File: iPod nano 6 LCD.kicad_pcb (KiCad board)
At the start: 2 copper layers, 5 parts, among them U1 AP5724

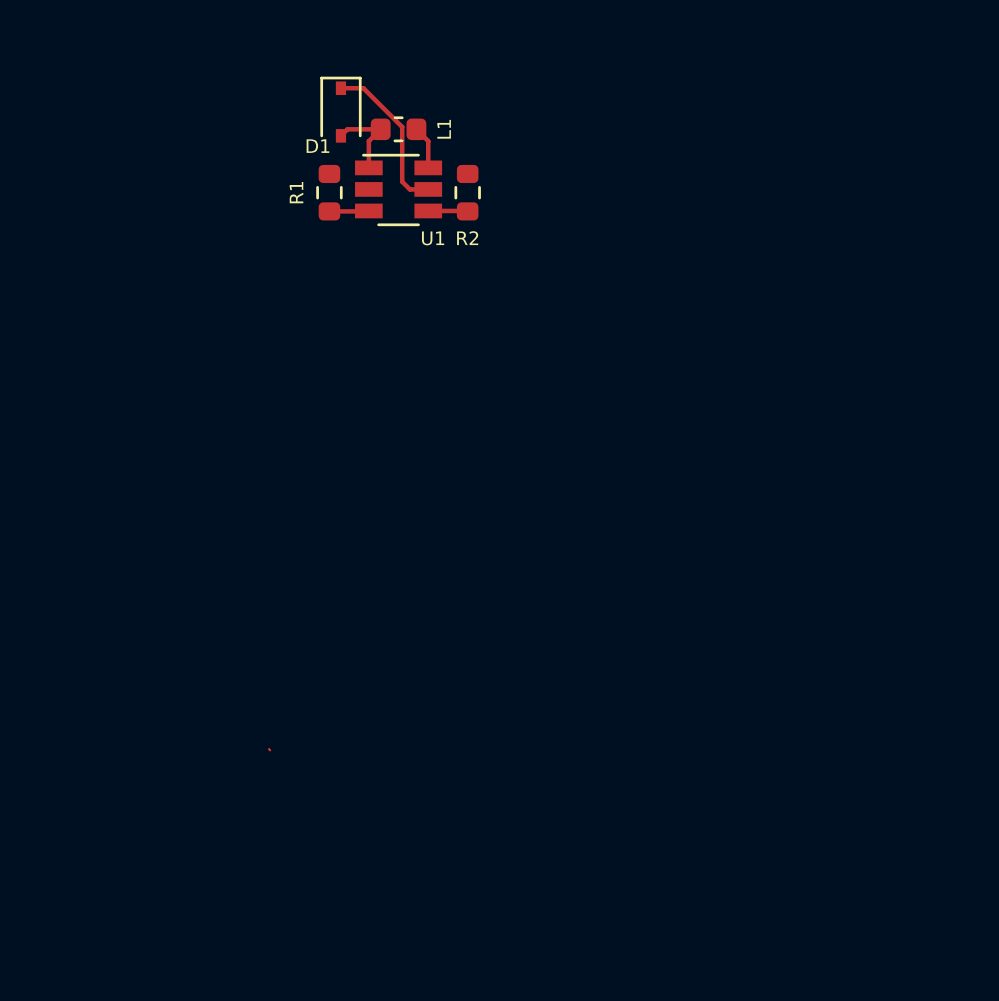
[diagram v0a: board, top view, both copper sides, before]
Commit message: Add USB and ATSAMD processor
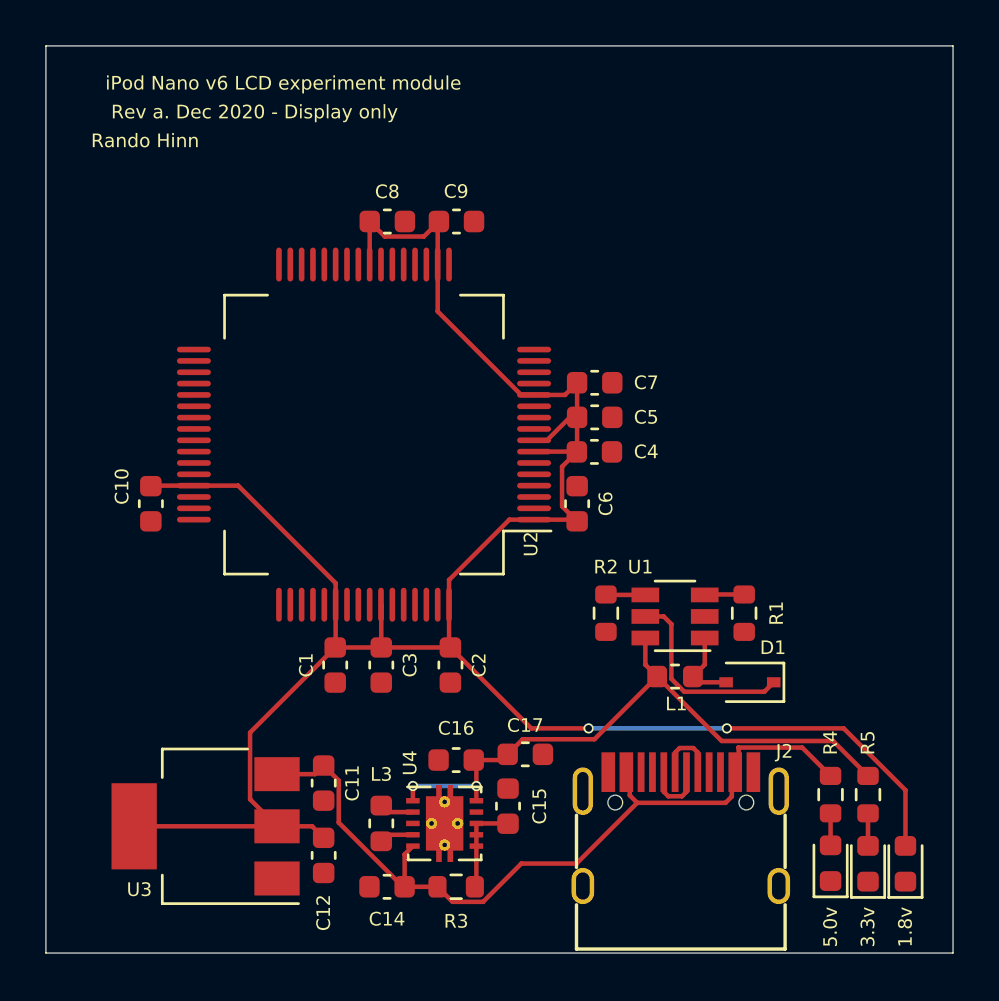
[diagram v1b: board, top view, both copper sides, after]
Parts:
- added C1: 1u, Capacitor_SMD:C_0603_1608Metric, F.Cu at (130.6, 85.1)
- added C10: 1u, Capacitor_SMD:C_0603_1608Metric, F.Cu at (122.4, 78.0)
- added C11: 1u, Capacitor_SMD:C_0603_1608Metric, F.Cu at (130.0, 90.3)
- added C12: 1u, Capacitor_SMD:C_0603_1608Metric, F.Cu at (130.0, 93.5)
- added C14: 1u, Capacitor_SMD:C_0603_1608Metric, F.Cu at (132.8, 94.9)
- added C15: .1u, Capacitor_SMD:C_0603_1608Metric, F.Cu at (138.2, 91.3)
- added C16: 10u, Capacitor_SMD:C_0603_1608Metric, F.Cu at (135.9, 89.3)
- added C17: 10u, Capacitor_SMD:C_0603_1608Metric, F.Cu at (138.9, 89.0)
- added C2: 1u, Capacitor_SMD:C_0603_1608Metric, F.Cu at (135.6, 85.1)
- added C3: 1u, Capacitor_SMD:C_0603_1608Metric, F.Cu at (132.6, 85.1)
- added C4: 1u, Capacitor_SMD:C_0603_1608Metric, F.Cu at (142.0, 75.7)
- added C5: 1u, Capacitor_SMD:C_0603_1608Metric, F.Cu at (142.0, 74.2)
- added C6: 1u, Capacitor_SMD:C_0603_1608Metric, F.Cu at (141.2, 78.0)
- added C7: 1u, Capacitor_SMD:C_0603_1608Metric, F.Cu at (142.0, 72.6)
- added C8: 1u, Capacitor_SMD:C_0603_1608Metric, F.Cu at (132.9, 65.5)
- added C9: 1u, Capacitor_SMD:C_0603_1608Metric, F.Cu at (135.9, 65.5)
- added D2: +5V, LED_SMD:LED_0603_1608Metric, F.Cu at (152.4, 93.8)
- added D3: +1.8V, LED_SMD:LED_0603_1608Metric, F.Cu at (155.7, 93.9)
- added D4: +3.3v, LED_SMD:LED_0603_1608Metric, F.Cu at (154.1, 93.9)
- added J2: USB_C_Receptacle_USB2.0, iPod nano 6 LCD:USB_C_Receptacle_GT-USB-7010, F.Cu at (145.8, 93.0)
- added L3: 2.2uH, Inductor_SMD:L_0603_1608Metric, F.Cu at (132.6, 92.1)
- added R3: 100, Resistor_SMD:R_0603_1608Metric, F.Cu at (135.9, 94.9)
- added R4: 16, Resistor_SMD:R_0603_1608Metric, F.Cu at (152.4, 90.8)
- added R5: 8, Resistor_SMD:R_0603_1608Metric, F.Cu at (154.1, 90.8)
- added U2: ATSAM3SD8BA-AU, iPod nano 6 LCD:QFP-64_12x12_Pitch0.5mm, F.Cu at (131.8, 74.9)
- added U3: AZ1117-1.8, Package_TO_SOT_SMD:SOT-223-3_TabPin2, F.Cu at (124.8, 92.2)
- added U4: TPS63001, Package_SON:Texas_DRC0010J_ThermalVias, F.Cu at (135.4, 92.1)
- moved D1 30.9 mm to (148.8, 85.9), turned to 180 degrees
- moved L1 27.0 mm to (145.5, 85.6), turned to 0 degrees
- moved R1 26.0 mm to (148.6, 82.8), turned to 270 degrees
- moved U1 22.4 mm to (145.5, 82.9), turned to 180 degrees
- moved R2 19.5 mm to (142.5, 82.8), turned to 270 degrees
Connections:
- net +3V0 renamed +3V3
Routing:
- net VDDIN: track 0.00 -> 101.9 mm, vias 0 -> 2
- net +5V: track 0.00 -> 35.9 mm
- net +3V3: track 1.92 -> 27.9 mm, vias 0 -> 2
- net Net-(C15-Pad1): track 0.00 -> 4.22 mm
- net Net-(J2-PadA7): track 0.00 -> 2.89 mm
- net Net-(J2-PadA6): track 0.00 -> 2.89 mm
- net Net-(L3-Pad2): track 0.00 -> 1.51 mm
- net Net-(L3-Pad1): track 0.00 -> 1.51 mm
- net LED+: track 7.11 -> 8.62 mm
- net Net-(D4-Pad2): track 0.00 -> 1.44 mm
- net Net-(D2-Pad2): track 0.00 -> 1.41 mm
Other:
- board outline added: 40 x 40 mm
- board text added: "1.8v"
- board text added: "3.3v"
- board text added: "5.0v"
- board text added: "Rando Hinn"
- board text added: "Rev a. Dec 2020 - Display only"
- board text added: "iPod Nano v6 LCD experiment module"

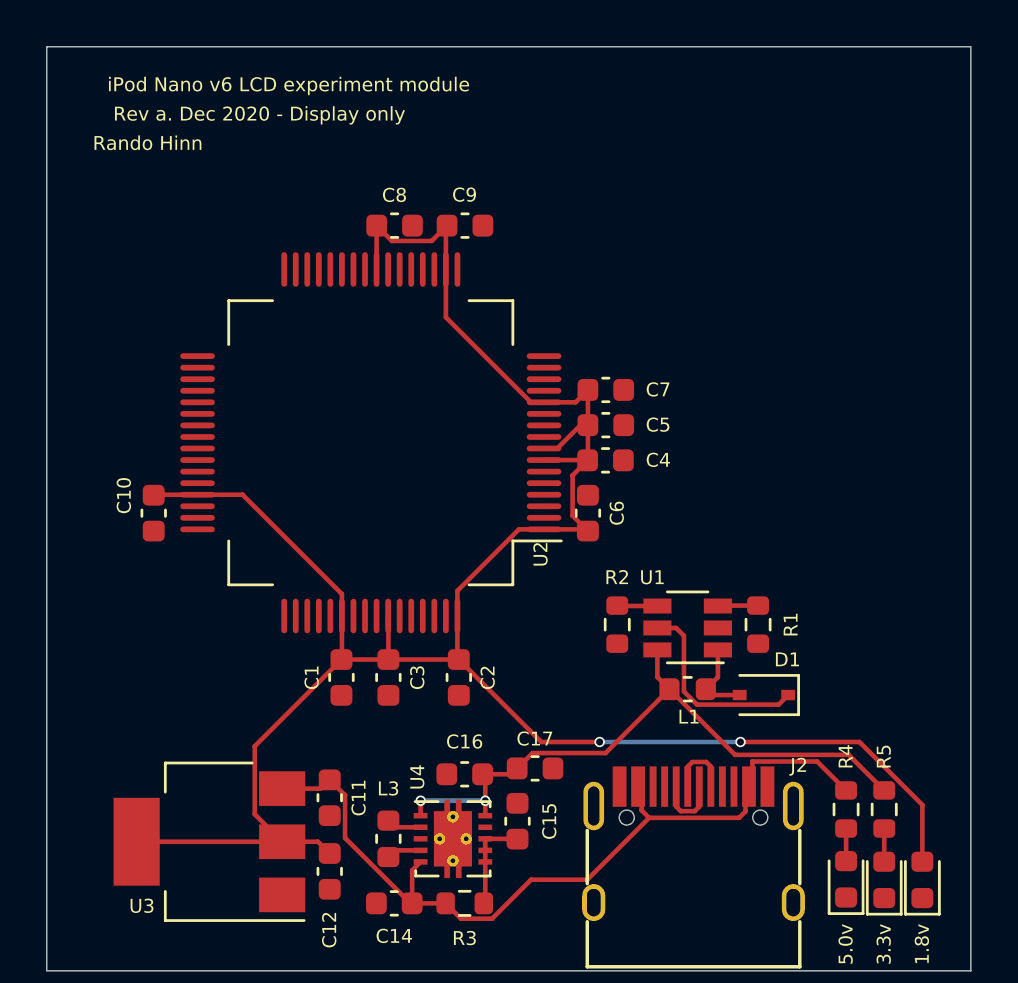
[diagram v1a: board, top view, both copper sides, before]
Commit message: Add JTAG and LCD connector and bias resistors
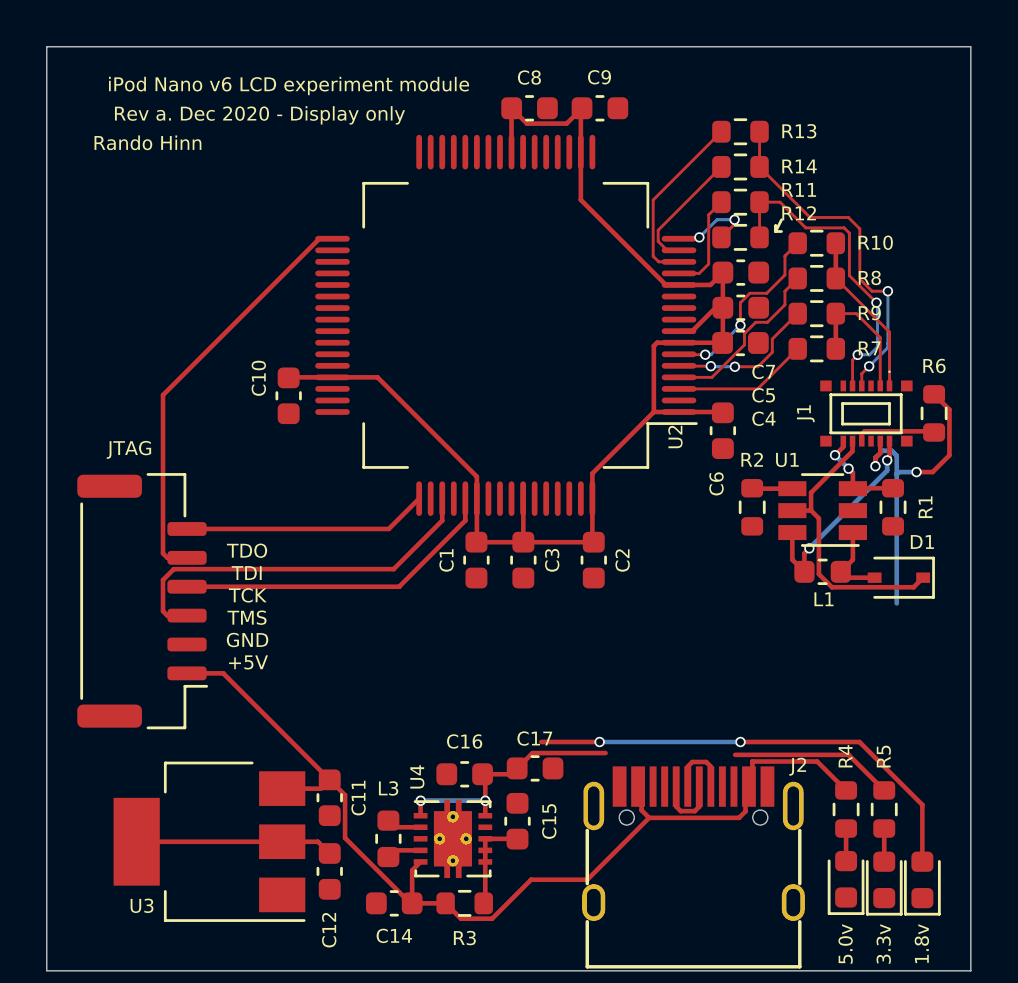
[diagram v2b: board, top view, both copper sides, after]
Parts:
- added J1: Molex_503548-1220, iPod nano 6 LCD:Molex 503548-1220, F.Cu at (153.2, 73.7)
- added J3: Conn_01x06_Male, Connector_JST:JST_GH_BM06B-GHS-TBT_1x06-1MP_P1.25mm_Vertical, F.Cu at (121.9, 81.8)
- added R10: 47, Resistor_SMD:R_0603_1608Metric, F.Cu at (151.1, 66.3)
- added R11: 220, Resistor_SMD:R_0603_1608Metric, F.Cu at (147.8, 64.5)
- added R12: 47, Resistor_SMD:R_0603_1608Metric, F.Cu at (147.8, 66.0)
- added R13: 220, Resistor_SMD:R_0603_1608Metric, F.Cu at (147.8, 61.5)
- added R14: 47, Resistor_SMD:R_0603_1608Metric, F.Cu at (147.8, 63.0)
- added R6: 10k, Resistor_SMD:R_0603_1608Metric, F.Cu at (156.2, 73.7)
- added R7: 220, Resistor_SMD:R_0603_1608Metric, F.Cu at (151.1, 70.9)
- added R8: 220, Resistor_SMD:R_0603_1608Metric, F.Cu at (151.1, 67.8)
- added R9: 47, Resistor_SMD:R_0603_1608Metric, F.Cu at (151.1, 69.3)
- moved C5 7.74 mm to (147.8, 69.1)
- moved C7 7.74 mm to (147.8, 67.6)
- moved U2 7.74 mm to (137.7, 69.8)
- moved C10 7.74 mm to (128.3, 72.9)
- moved C2 7.74 mm to (141.5, 80.0)
- moved C3 7.74 mm to (138.4, 80.0)
- moved C4 7.74 mm to (147.8, 70.6)
- moved C8 7.74 mm to (138.7, 60.5)
- moved C9 7.74 mm to (141.7, 60.5)
- moved D1 7.74 mm to (154.7, 80.8)
- moved R2 7.74 mm to (148.3, 77.7)
- moved C1 7.74 mm to (136.4, 80.0)
- moved L1 7.74 mm to (151.4, 80.5)
- moved R1 7.74 mm to (154.4, 77.7)
- moved U1 7.74 mm to (151.4, 77.9)
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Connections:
- U2 pad 3: Net-(U2-Pad3) -> IC_CLKN
- U2 pad 33: Net-(U2-Pad33) -> TDI
- U2 pad 4: Net-(U2-Pad4) -> IC_CLKP
- U2 pad 49: Net-(U2-Pad49) -> TDO
- U2 pad 51: Net-(U2-Pad51) -> TMS
- U2 pad 53: Net-(U2-Pad53) -> TCK
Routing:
- net TDI: track 0.00 -> 18.1 mm
- net TMS: track 0.00 -> 16.6 mm
- net DP: track 0.00 -> 15.1 mm, vias 0 -> 2
- net TCK: track 0.00 -> 14.2 mm
- net DN: track 0.00 -> 13.8 mm, vias 0 -> 2
- net TDO: track 0.00 -> 10.6 mm
- net Net-(R10-Pad1): track 0.00 -> 8.20 mm, vias 0 -> 2
- net +5V: track 35.9 -> 44.0 mm
- net Net-(R13-Pad1): track 0.00 -> 7.83 mm
- net IC_CLKP: track 0.00 -> 7.54 mm
- net CLKP: track 0.00 -> 7.14 mm
- net Net-(R9-Pad1): track 0.00 -> 6.44 mm, vias 0 -> 2
- net CLKN: track 0.00 -> 5.97 mm
- net IC_CLKN: track 0.00 -> 5.86 mm
- net Net-(R14-Pad1): track 0.00 -> 5.42 mm
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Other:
- board text added: "JTAG"
- board text added: "TDO TDI TCK TMS GND +5V"

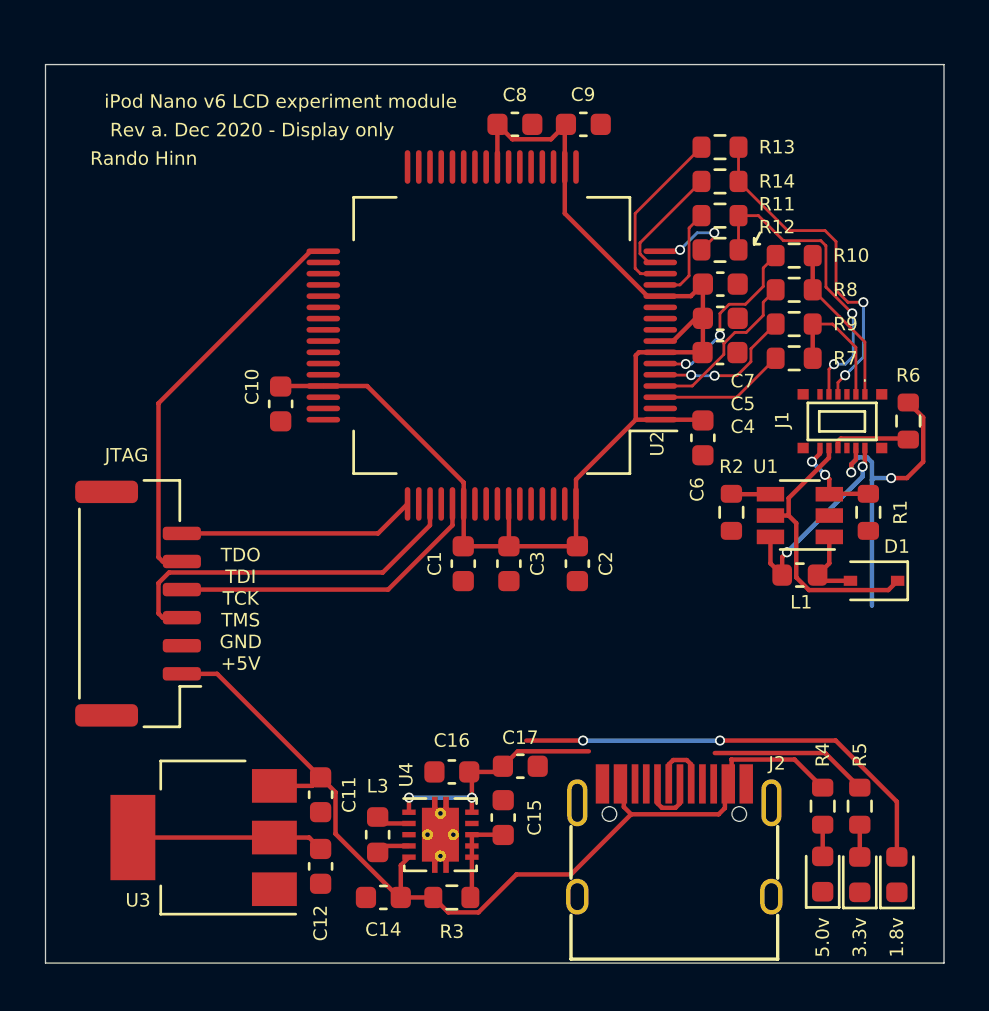
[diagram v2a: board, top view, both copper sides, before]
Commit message: Add the 2 crystals on board
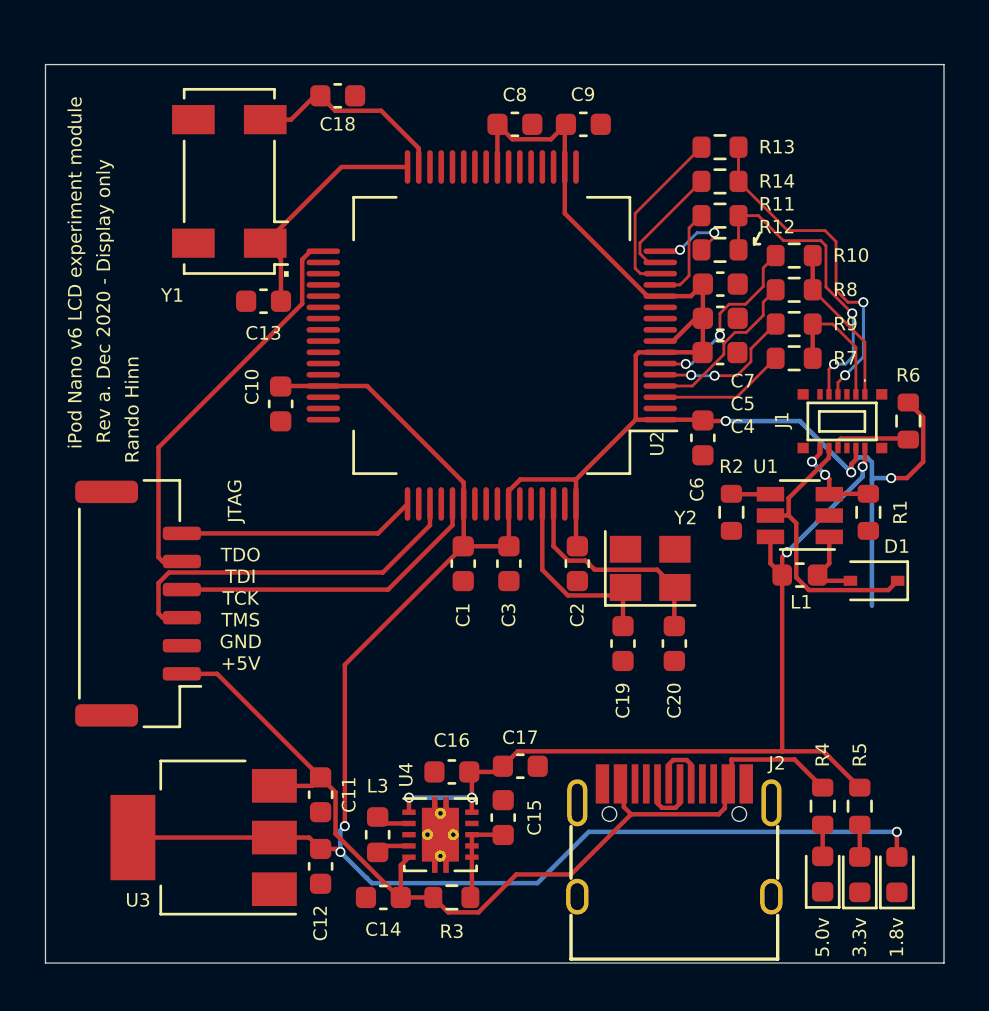
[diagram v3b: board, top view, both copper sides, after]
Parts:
- added C13: 12.5p, Capacitor_SMD:C_0603_1608Metric, F.Cu at (127.5, 68.3)
- added C18: 12.5p, Capacitor_SMD:C_0603_1608Metric, F.Cu at (130.8, 59.2)
- added C19: 10p, Capacitor_SMD:C_0603_1608Metric, F.Cu at (143.5, 83.6)
- added C20: 10p, Capacitor_SMD:C_0603_1608Metric, F.Cu at (145.8, 83.6)
- added Y1: 32.768k, Crystal:Crystal_SMD_Abracon_ABS25-4Pin_8.0x3.8mm, F.Cu at (126.0, 63.0)
- added Y2: 20MHz, Crystal:Crystal_SMD_Abracon_ABM8G-4Pin_3.2x2.5mm, F.Cu at (144.7, 80.2)
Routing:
- net VDDIN: track 101.9 -> 134.4 mm, vias 4 -> 6
- net +3V3: track 27.2 -> 40.9 mm
- net Net-(C13-Pad1): track 0.00 -> 10.6 mm
- net Net-(C20-Pad1): track 0.00 -> 9.78 mm
- net Net-(C18-Pad1): track 0.00 -> 9.07 mm
- net Net-(C19-Pad1): track 0.00 -> 9.03 mm
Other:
- board text added: "."

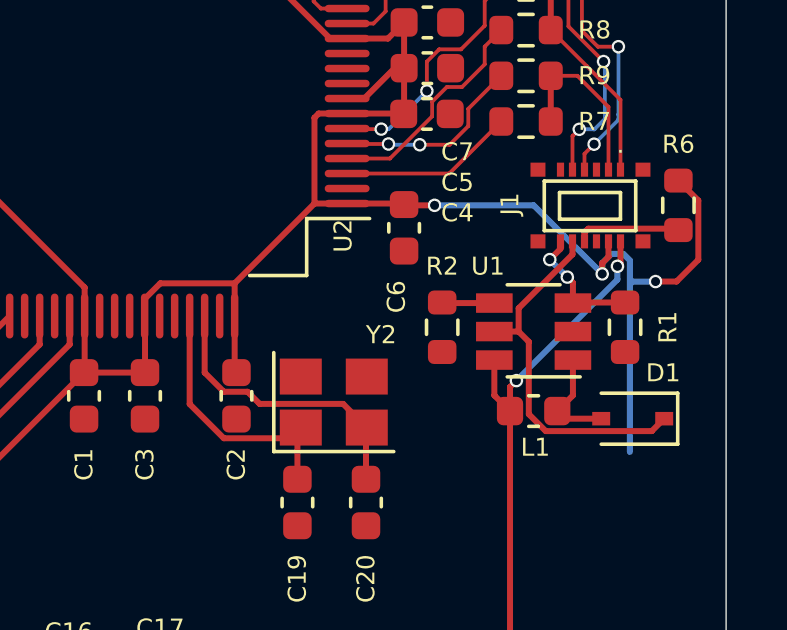
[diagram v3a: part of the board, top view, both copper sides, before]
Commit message: Add Symbol for XTSD04GLGEAG
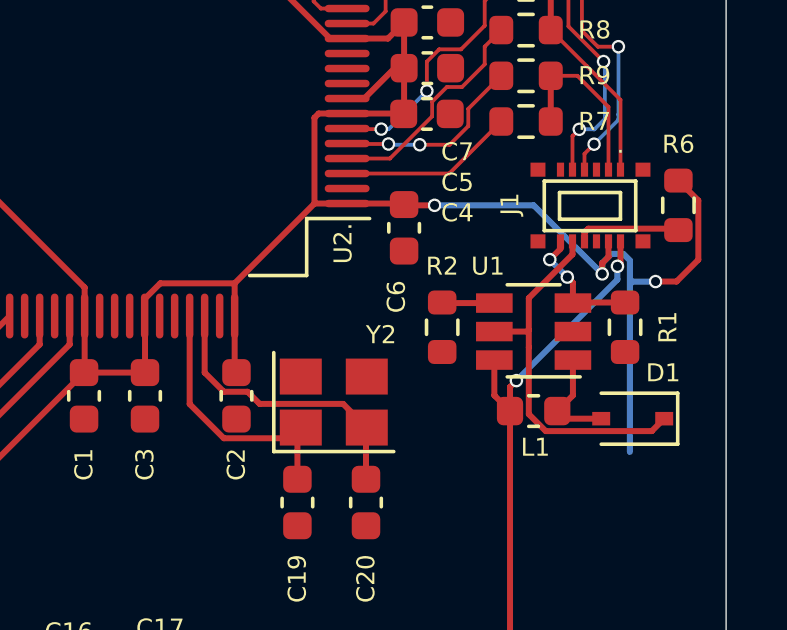
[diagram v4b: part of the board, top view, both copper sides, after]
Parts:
- renumbered U2 to U2.
